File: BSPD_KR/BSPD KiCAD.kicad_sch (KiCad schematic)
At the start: 65 parts, among them J1 Conn_01x03, J2 Conn_01x02, J3 Conn_01x02, K1 G5Q-1A4-DC12, Q1 2N7002, Q3 2N7002, U18 SN74AHCT1G08DBVR, U19 LM339N, U4 LM7805MPX/NOPB, U5 LM339N, U6 SN74AHC1G02DBVR, U9 SN74LVC1G04DBVT

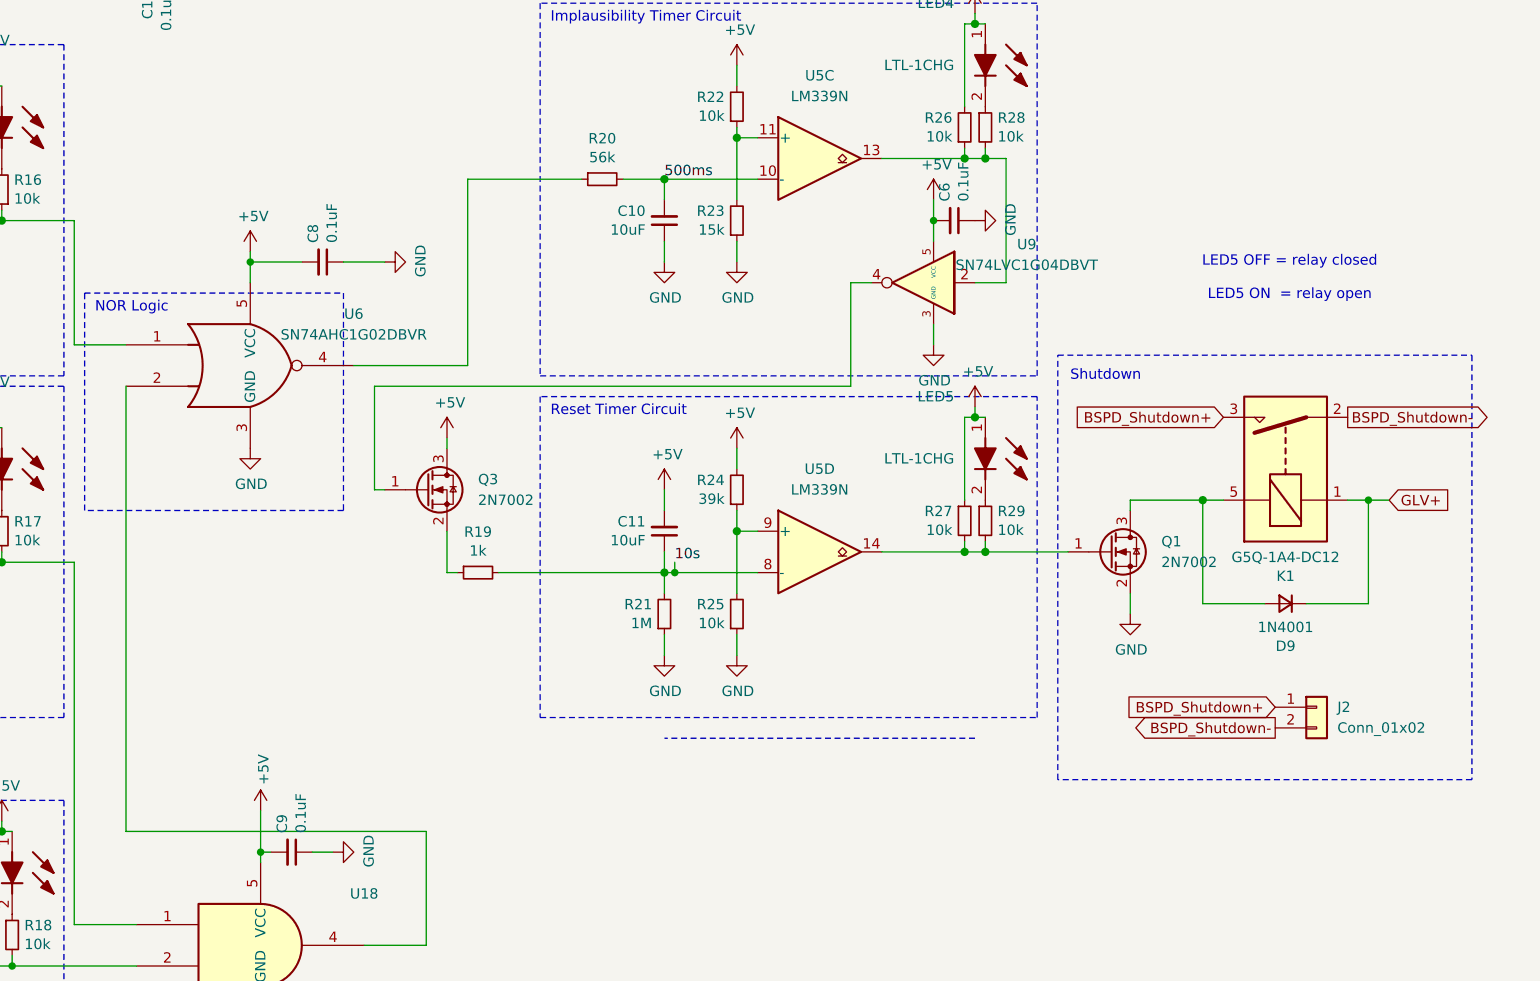
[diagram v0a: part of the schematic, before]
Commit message: fix(bspd): replace 10s RC self-reset with SR latch, tighten 500ms timer
Reset timer hold time depended on Q3 Vgs(th) and electrolytic tolerance:
6.8-13.6s against FSUK T11.6.1 minimum of 10s. Replaced with a NOR SR
latch (U20/U21, SN74AHC1G02) that holds the SDC open until LVMS power
cycle, with POR network C13/R30/D10 to clear it at power-up. R20 56k->39k
so the 500ms implausibility timer trips at 0.29-0.43s worst case (T11.6.2).

Co-Authored-By: Claude Fable 5.1 <noreply@anthropic.com>
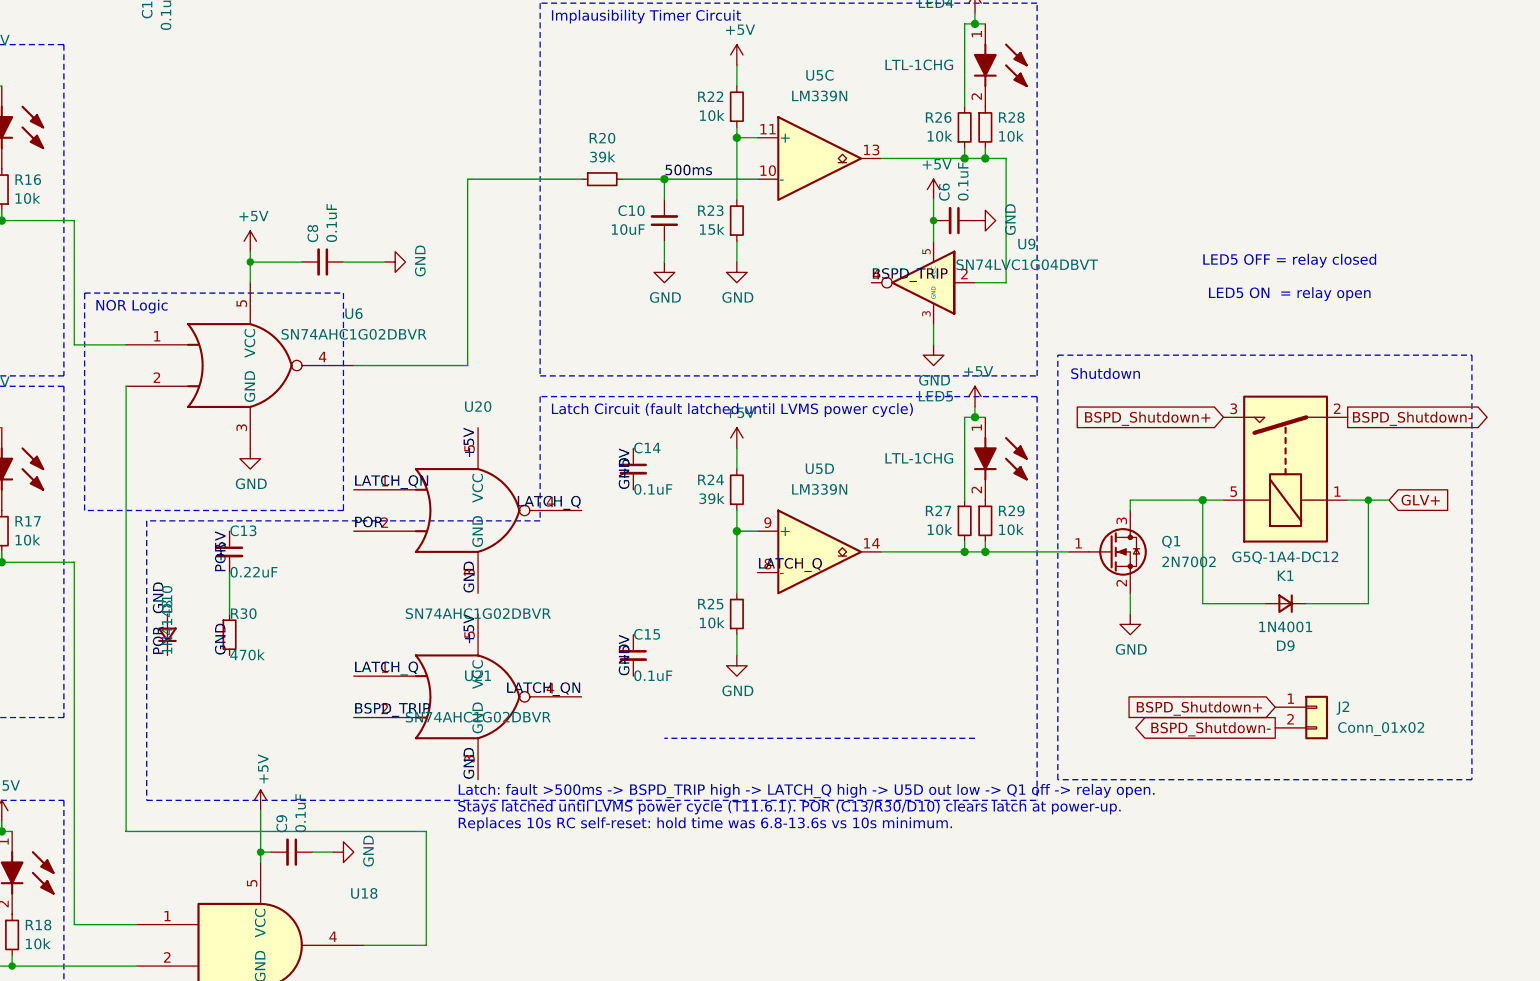
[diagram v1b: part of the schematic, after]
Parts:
- removed C11: 10uF, Capacitor_THT:CP_Radial_D5.0mm_P2.50mm, symbol Device:C_Small
- removed Q3: 2N7002, Package_TO_SOT_SMD:SOT-23, symbol Transistor_FET:2N7002
- removed R19: 1k, Resistor_THT:R_Axial_DIN0207_L6.3mm_D2.5mm_P10.16mm_Horizontal, symbol Device:R_Small
- removed R21: 1M, Resistor_THT:R_Axial_DIN0207_L6.3mm_D2.5mm_P10.16mm_Horizontal, symbol Device:R_Small
- added C13: 0.22uF, Kicad_Libraries:FA14X7R1H224KNU00, symbol Device:C_Small
- added C14, C15: 0.1uF, Kicad_Libraries:FA18X7R1H104KNU00, symbol Device:C_Small
- added D10: 1N4148, Diode_THT:D_DO-35_SOD27_P7.62mm_Horizontal, symbol Device:D_Small
- added R30: 470k, Resistor_THT:R_Axial_DIN0207_L6.3mm_D2.5mm_P10.16mm_Horizontal, symbol Device:R_Small
- added U20, U21: SN74AHC1G02DBVR, Package_TO_SOT_SMD:SOT-23-5, symbol 74xGxx:74AHC1G02
- R20: value 56k -> 39k; Part Number MCF 0.25W 56K -> MCF 0.25W 39K
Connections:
- net +5V: now also C13.1, C14.1, C15.1, U20.5 (VCC), U21.5 (VCC)
- net GND: now also C14.2, C15.2, D10.2 (A), R30.2, U20.3 (GND), U21.3 (GND)
- net BSPD_TRIP: now reaches U9.4
- net BSPD_TRIP: now also U21.2
- net 10s renamed LATCH_Q
- net LATCH_Q: now also U20.4, U21.1
- new net LATCH_QN: U20.1, U21.4
- new net POR: C13.2, D10.1 (K), R30.1, U20.2
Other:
- note added: "Latch Circuit (fault latched until LVMS power cycle)"
- note added: "Latch: fault >500ms -> BSPD_TRIP high -> LATCH_Q high -> U5D out low -> Q1 off -> relay open. Stays latched until LVMS power cycle (T11.6.1). POR (C13/R30/D10) clears latch at power-up. Replaces 10s RC self-reset: hold time was 6.8-13.6s vs 10s minimum."
- note removed: "Reset Timer Circuit"

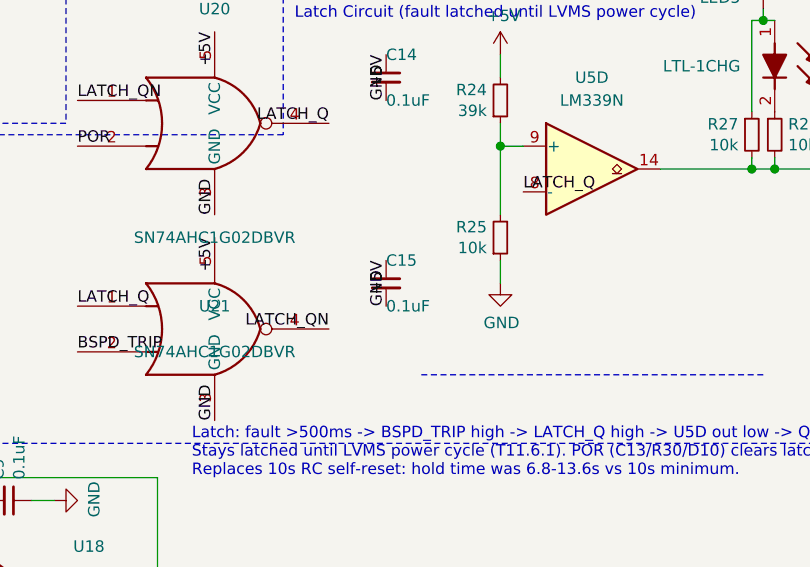
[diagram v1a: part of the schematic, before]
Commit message: feat(bspd): lay out SR latch on PCB, fix board outline and via drill
Place U20/U21 (SN74AHC1G02 latch) on the bottom side under R30/D10,
R30/D10/C13 on the freed R19/R21/C11 sites and C14 decoupling below.
Route the new nets with Freerouting; existing nets unchanged within
1.5 mm. Drop C15 (one shared decoupling cap is enough for two adjacent
gates) and switch D10 to the DO-41 footprint already used by D9.

Also close the Edge.Cuts outline (small endpoint mismatches made the
Specctra exporter reject the board) and raise via drill to 0.3 mm to
meet the board's own min-hole constraint. DRC: 0 errors, 0 unconnected.

Co-Authored-By: Claude Fable 5.1 <noreply@anthropic.com>
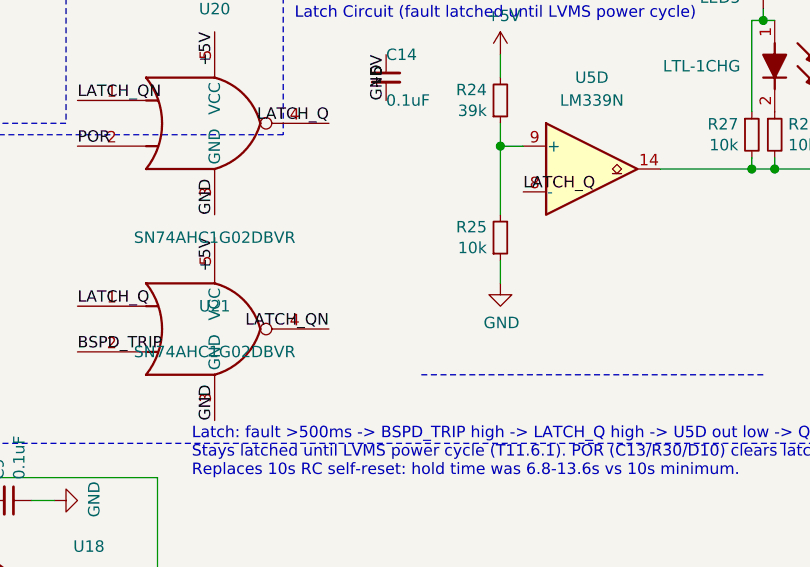
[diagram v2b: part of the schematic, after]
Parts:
- removed C15: 0.1uF, Kicad_Libraries:FA18X7R1H104KNU00, symbol Device:C_Small
- D10: footprint Diode_THT:D_DO-35_SOD27_P7.62mm_Horizontal -> Diode_THT:D_DO-41_SOD81_P10.16mm_Horizontal
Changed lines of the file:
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@@
 			)
 		)
-		(property "Footprint" "Diode_THT:D_DO-35_SOD27_P7.62mm_Horizontal"
+		(property "Footprint" "Diode_THT:D_DO-41_SOD81_P10.16mm_Horizontal"
 			(at 228.6 137.16 90)
 			(hide yes)
@@
 			)
 		)
-	)
-	(symbol
-		(lib_id "Device:C_Small")
-		(at 285.75 139.7 0)
-		(unit 1)
-		(body_style 1)
-		(exclude_from_sim no)
-		(in_bom yes)
-		(on_board yes)
-		(in_pos_files yes)
-		(dnp no)
-		(property "Reference" "C15"
-			(at 285.75 137.16 0)
-			(show_name no)
-			(do_not_autoplace no)
-			(effects
-				(font
-					(size 1.27 1.27)
-				)
-				(justify left)
-			)
-		)
-		(property "Value" "0.1uF"
-			(at 285.75 142.24 0)
-			(show_name no)
-			(do_not_autoplace no)
-			(effects
-				(font
-					(size 1.27 1.27)
-				)
-				(justify left)
-			)
-		)
-		(property "Footprint" "Kicad_Libraries:FA18X7R1H104KNU00"
-			(at 285.75 139.7 0)
-			(hide yes)
-			(show_name no)
-			(do_not_autoplace no)
-			(effects
-				(font
-					(size 1.27 1.27)
-				)
-			)
-		)
-		(property "Datasheet" "https://www.farnell.com/datasheets/2923220.pdf"
-			(at 285.75 139.7 0)
-			(hide yes)
-			(show_name no)
-			(do_not_autoplace no)
-			(effects
-				(font
-					(size 1.27 1.27)
-				)
-			)
-		)
-		(property "Description" "Unpolarized capacitor, small symbol"
-			(at 285.75 139.7 0)
-			(hide yes)
-			(show_name no)
-			(do_not_autoplace no)
-			(effects
-				(font
-					(size 1.27 1.27)
-				)
-			)
-		)
-		(property "Part Number" "FA18X7R1H104KNU00"
-			(at 285.75 139.7 0)
-			(effects
-				(font
-					(size 1.27 1.27)
-				)
-				(hide yes)
-			)
-		)
-		(pin "1"
-		)
-		(pin "2"
-		)
-		(instances
-			(project "BSPD KiCAD"
-				(path "/a06e8e78-f567-42e6-b645-013b1073ca31"
-					(reference "C15")
-					(unit 1)
-				)
-			)
-		)
-	)
-	(text "Latch: fault >500ms -> BSPD_TRIP high -> LATCH_Q high -> U5D out low -> Q1 off -> relay open.\nStays latched until LVMS power cycle (T11.6.1). POR (C13/R30/D10) clears latch at power-up.\nReplaces 10s RC self-reset: hold time was 6.8-13.6s vs 10s minimum."
+	)	(text "Latch: fault >500ms -> BSPD_TRIP high -> LATCH_Q high -> U5D out low -> Q1 off -> relay open.\nStays latched until LVMS power cycle (T11.6.1). POR (C13/R30/D10) clears latch at power-up.\nReplaces 10s RC self-reset: hold time was 6.8-13.6s vs 10s minimum."
 		(exclude_from_sim no)
 		(at 264.16 161.29 0)
@@
 		(effects
 			(font
-				(size 1.27 1.27)
-			)
-			(justify left bottom)
-		)
-	)
-	(label "+5V"
-		(at 285.75 137.16 270)
-		(effects
-			(font
-				(size 1.27 1.27)
-			)
-			(justify right bottom)
-		)
-	)
-	(label "GND"
-		(at 285.75 142.23999999999998 90)
-		(effects
-			(font

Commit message: fix(bspd): correct C10 electrolytic polarity, harden POR, enforce 0.25mm tracks
Full-chain behavioural sim (analysis/helpers/bspd_system.cir) showed the
POR pulse (220n/470k) could fall short of the AHC input threshold on a
slow 5V ramp, leaving the latch powered up in the tripped state. C13 is
now 10uF/100k (tau 1s), passing the worst-case ramp with margin.

The same pass found C10 (500ms timer cap) fitted with its positive pad on
GND while the timer node swings 0-5V; swapped the symbol orientation and
pad nets so the cap is forward biased. C13 uses the same part and
footprint. J2 nudged 0.5mm to clear the larger cap.

Re-routed the new nets with Freerouting at the board's 0.25mm minimum
track width (netclass default was 0.2, below the constraint). DRC: 0
errors, 0 unconnected; all pad nets match the schematic netlist.

Co-Authored-By: Claude Fable 5.1 <noreply@anthropic.com>
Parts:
- C13: value 0.22uF -> 10uF; footprint Kicad_Libraries:FA14X7R1H224KNU00 -> Capacitor_THT:CP_Radial_D5.0mm_P2.50mm; Part Number FA14X7R1H224KNU00 -> ECE-A1EKA100I
- R30: value 470k -> 100k; Part Number MCF 0.25W 470K -> MCF 0.25W 100K
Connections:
- net 500ms: now also C10.1; no longer C10.2
- net GND: now also C10.2; no longer C10.1
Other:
- moved on the sheet: C10
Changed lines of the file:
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@@
 	(symbol
 		(lib_id "Device:C_Small")
-		(at 289.56 86.36 0)
+		(at 289.56 86.36 180)
 		(mirror x)
 		(unit 1)
@@
 			)
 		)
-		(property "Value" "0.22uF"
+		(property "Value" "10uF"
 			(at 236.22 129.54 0)
 			(show_name no)
@@
 			)
 		)
-		(property "Footprint" "Kicad_Libraries:FA14X7R1H224KNU00"
+		(property "Footprint" "Capacitor_THT:CP_Radial_D5.0mm_P2.50mm"
 			(at 236.22 127 0)
 			(hide yes)
@@
 			)
 		)
-		(property "Datasheet" ""
+		(property "Datasheet" "https://industrial.panasonic.com/cdbs/www-data/pdf/RDF0000/ABA0000C1050.pdf"
 			(at 236.22 127 0)
 			(hide yes)
@@
 			)
 		)
-		(property "Part Number" "FA14X7R1H224KNU00"
+		(property "Part Number" "ECE-A1EKA100I"
 			(at 236.22 127 0)
 			(effects
@@
 			)
 		)
-		(property "Value" "470k"
+		(property "Value" "100k"
 			(at 236.22 139.7 0)
 			(show_name no)
@@
 			)
 		)
-		(property "Part Number" "MCF 0.25W 470K"
+		(property "Part Number" "MCF 0.25W 100K"
 			(at 236.22 137.16 0)
 			(effects

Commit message: feat(bspd): trip on any single sensor fault, lower missing threshold
An unplugged, open or shorted sensor did not trip the BSPD on its own:
the "sensor missing" comparators were wired-OR into the same wires as
"pressure/current too high", so a dead brake sensor looked like hard
braking and the board waited for high current (and vice versa).
T11.9.2 requires open circuit, short to ground and short to supply on
any SCS to reach the safe state (open SDC).

U5B, U19B and U19D now drive a separate FAULT_N net instead of the
per-sensor wires. Two LM393s (SOIC-8, bottom side, inside the U5/U19
footprints) add over-range checks at 4.74 V for all three sensors on
the same net. R32/C15 debounce FAULT_N (~0.16 s, glitches up to
~0.12 s ignored) and U22B pulls TRIP_REQ_N low, joining the existing
timer output, so a sensor fault latches exactly like an implausibility.

R8/R10/R12 go from 10k to 5.1k, moving the missing threshold from
0.45 V to 0.24 V: the TE M7139 brake sensors sit at 0.5 V at rest,
leaving only 0.05 V of margin before.

PCB: 10 new bottom-side parts. The three moved outputs were branch
points of their sensor wires, so those three spots were rerouted by
hand. New nets were routed with Freerouting with all existing tracks
locked; existing copper is otherwise unchanged. DRC 0 errors and 0
unconnected; parity shows only the H1-H4 mounting holes; the warning
set matches the previous board.

Sim: shared model in bspd_core.inc; bspd_fault_tests.cir covers each
sensor unplugged or shorted to 5 V (all trip in 0.16 s), 50/120 ms
glitches, full-scale and 30 bar braking alone, and late sensor
power-up (none trip). The original timeline results are unchanged.

Regenerated BOMs, fab outputs and the STEP model, which had dated
from before the latch rework. README updated, including the open item
that the current sensor must stay below 4.74 V (~224 A at 10 mV/A).

Co-Authored-By: Claude Opus 5.5 <noreply@anthropic.com>
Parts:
- added C15: 1uF, Capacitor_SMD:C_0805_2012Metric, symbol Device:C_Small
- added C16: 0.1uF, Capacitor_SMD:C_0805_2012Metric, symbol Device:C_Small
- added R31: 10k, Resistor_SMD:R_0805_2012Metric, symbol Device:R_Small
- added R32: 100k, Resistor_SMD:R_0805_2012Metric, symbol Device:R_Small
- added R33, R35: 1k, Resistor_SMD:R_0805_2012Metric, symbol Device:R_Small
- added R34, R36: 18k, Resistor_SMD:R_0805_2012Metric, symbol Device:R_Small
- added U22, U23: LM393, Package_SO:SOIC-8_3.9x4.9mm_P1.27mm, symbol Comparator:LM393
- R10, R12, R8: value 10k -> 5.1k; Part Number MCF 0.25W 10K -> MCF 0.25W 5K1
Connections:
- net +5V: now also R31.1, R33.1, R35.1
- net GLV+: now also C16.1, U22.8 (V+), U23.8 (V+)
- net GND: now also C15.2, C16.2, R34.2, R36.2, U22.4 (V-), U23.4 (V-)
- net at R14.1, R17.2, U18.1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: no longer U19.1
- net at R13.1, R16.1, U5.2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: no longer U5.1
- net TRIP_REQ_N: now reaches R26.1, R28.2, U5.13, U9.2
- net TRIP_REQ_N: now also U22.7
- net REF_1V0: now reaches R24.1, R25.2, U5.9 (+)
- net REF_1V0: now also U22.6 (-)
- net SENS_CUR: now reaches R4.1, TP1.1, U5.4 (-), U5.7 (+)
- net SENS_CUR: now also U22.2 (-)
- net SENS_FRONT: now reaches R5.1, TP2.1, U19.4 (-), U19.7 (+)
- net SENS_FRONT: now also U23.2 (-)
- net at R15.1, R18.2, U18.2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: no longer U19.14
- net SENS_REAR: now reaches R6.1, TP3.1, U19.10 (-), U19.9 (+)
- net SENS_REAR: now also U23.6 (-)
- new net FAULT_F: C15.1, R32.2, U22.5 (+)
- new net FAULT_N: R31.2, R32.1, U19.1, U19.14, U22.1, U23.1, U23.7, U5.1
- new net OVR_REF_BRK: R35.2, R36.1, U23.3 (+), U23.5 (+)
- new net OVR_REF_CUR: R33.2, R34.1, U22.3 (+)
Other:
- note added: "Below 0.24 V or above 4.74 V = sensor fault (trips the BSPD) 20 bar corresponds 2.8V 25 bar corresponds to 3.36V 30 bar correspons to 3.93v"
- note added: "Sensor Fault Detection (T11.9.2): a sensor reading below 0.24 V (open circuit, short to GND) or above 4.74 V (short to supply) pulls FAULT_N low (under-range: U5B, U19B, U19D; over-range: U22A, U23A, U23B). R32/C15 debounce it (~0.17 s), then U22B pulls TRIP_REQ_N low -> U9 -> BSPD_TRIP -> latch (until LVMS power cycle). OVR_REF = 5 V x 18k/19k = 4.74 V. U22/U23 are SOIC-8 on the bottom side, ins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"
- note removed: "Anything below 0.455 volts is invalid 20 bar corresponds 2.8V 25 bar corresponds to 3.36V 30 bar correspons to 3.93v"
